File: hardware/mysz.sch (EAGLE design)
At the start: 30 parts, among them IC1 LM1117T(H)-3.3, IC2 LM1117T(H)-3.3, U1 NUCLEO-L053R8

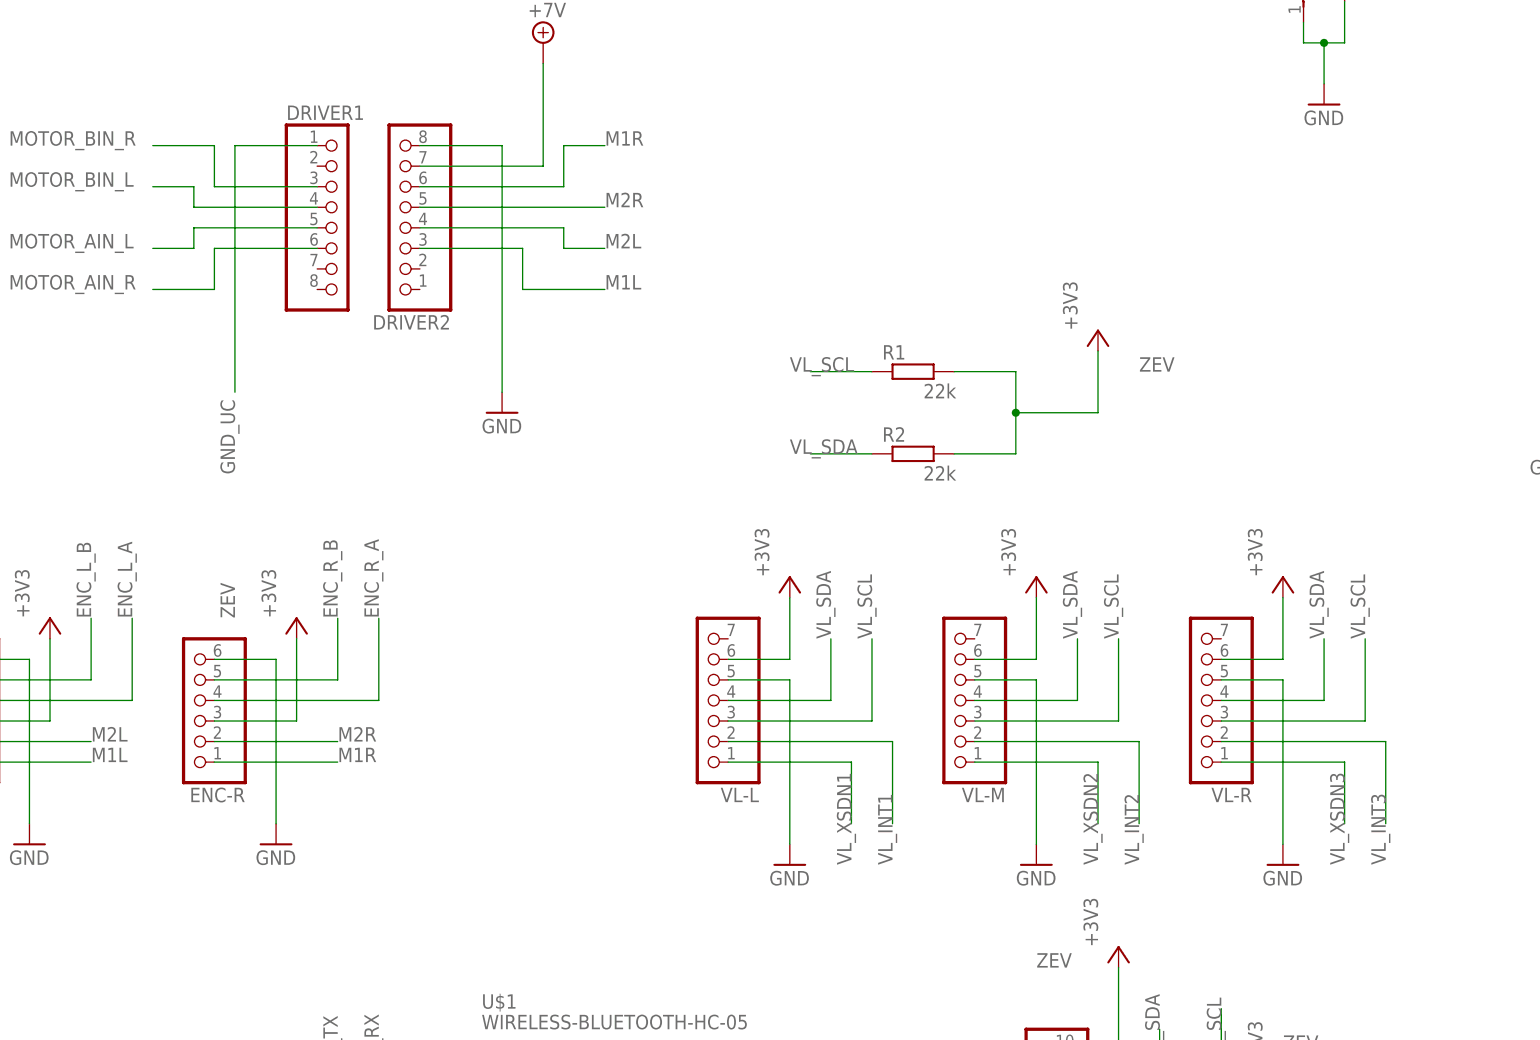
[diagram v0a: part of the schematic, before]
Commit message: Added missing links.sch
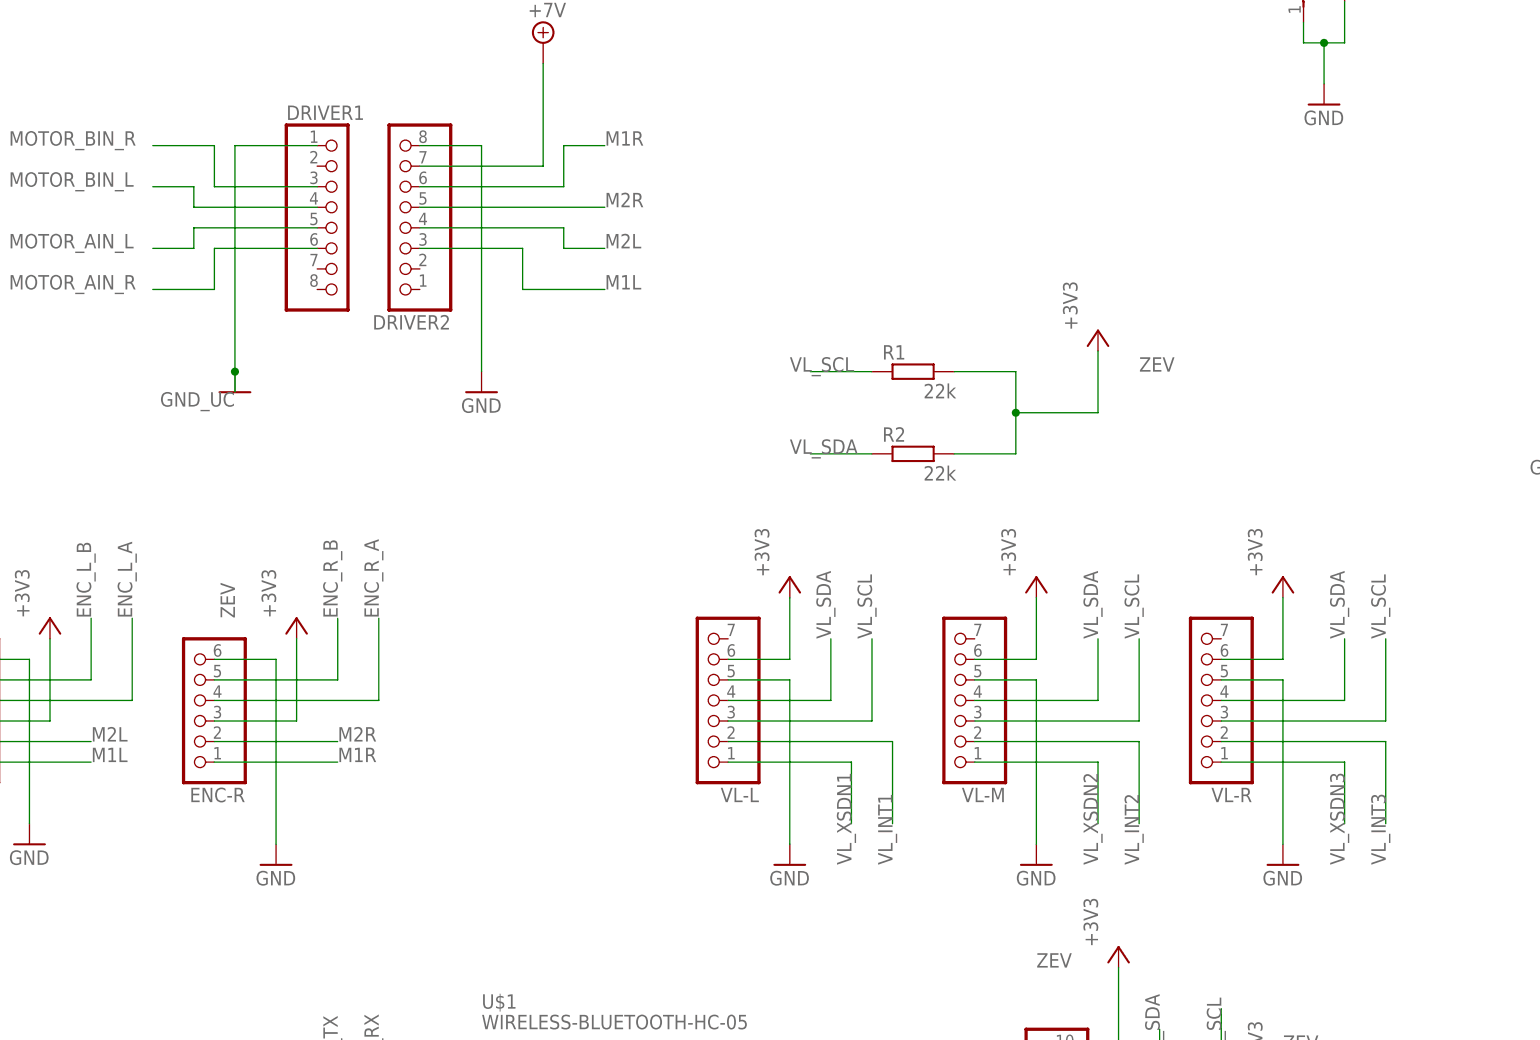
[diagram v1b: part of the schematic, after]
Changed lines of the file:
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@@
 <part name="+3V13" library="supply1" library_urn="urn:adsk.eagle:library:371" deviceset="+3V3" device=""/>
 <part name="C9" library="capacitor-wima" library_urn="urn:adsk.eagle:library:116" deviceset="C" device="2,5-3" package3d_urn="urn:adsk.eagle:package:5436/1" value="100nF"/>
+<part name="GND13" library="supply1" library_urn="urn:adsk.eagle:library:371" deviceset="GND" device=""/>
 </parts>
 <sheets>
@@
 <attribute name="VALUE" x="7.62" y="83.82" size="1.778" layer="96" rot="R90"/>
 </instance>
-<instance part="GND4" gate="1" x="7.62" y="55.88" smashed="yes">
-<attribute name="VALUE" x="5.08" y="53.34" size="1.778" layer="96"/>
+<instance part="GND4" gate="1" x="7.62" y="53.34" smashed="yes">
+<attribute name="VALUE" x="5.08" y="50.8" size="1.778" layer="96"/>
 </instance>
 <instance part="GND5" gate="1" x="71.12" y="53.34" smashed="yes">
@@
 <attribute name="VALUE" x="29.21" y="147.32" size="1.778" layer="96" rot="R180"/>
 </instance>
-<instance part="GND9" gate="1" x="35.56" y="109.22" smashed="yes">
-<attribute name="VALUE" x="33.02" y="106.68" size="1.778" layer="96"/>
+<instance part="GND9" gate="1" x="33.02" y="111.76" smashed="yes">
+<attribute name="VALUE" x="30.48" y="109.22" size="1.778" layer="96"/>
 </instance>
 <instance part="SUPPLY2" gate="G$1" x="40.64" y="154.94" smashed="yes">
@@
 <attribute name="VALUE" x="141.224" y="160.401" size="1.778" layer="96"/>
 </instance>
+<instance part="GND13" gate="1" x="2.54" y="111.76" smashed="yes"/>
 </instances>
 <busses>
@@
 <pinref part="ENC-R" gate="A" pin="6"/>
 <wire x1="0" y1="78.74" x2="7.62" y2="78.74" width="0.1524" layer="91"/>
-<wire x1="7.62" y1="78.74" x2="7.62" y2="58.42" width="0.1524" layer="91"/>
+<wire x1="7.62" y1="78.74" x2="7.62" y2="55.88" width="0.1524" layer="91"/>
 <pinref part="GND4" gate="1" pin="GND"/>
 </segment>
@@
 <segment>
 <pinref part="DRIVER2" gate="A" pin="8"/>
-<wire x1="25.4" y1="142.24" x2="35.56" y2="142.24" width="0.1524" layer="91"/>
-<wire x1="35.56" y1="142.24" x2="35.56" y2="111.76" width="0.1524" layer="91"/>
+<wire x1="25.4" y1="142.24" x2="33.02" y2="142.24" width="0.1524" layer="91"/>
+<wire x1="33.02" y1="142.24" x2="33.02" y2="114.3" width="0.1524" layer="91"/>
 <pinref part="GND9" gate="1" pin="GND"/>
 </segment>
@@
 <segment>
 <pinref part="VL-M" gate="A" pin="4"/>
-<wire x1="93.98" y1="73.66" x2="106.68" y2="73.66" width="0.1524" layer="91"/>
-<wire x1="106.68" y1="73.66" x2="106.68" y2="81.28" width="0.1524" layer="91"/>
-<label x="106.68" y="81.28" size="1.778" layer="95" rot="R90"/>
+<wire x1="93.98" y1="73.66" x2="109.22" y2="73.66" width="0.1524" layer="91"/>
+<wire x1="109.22" y1="73.66" x2="109.22" y2="81.28" width="0.1524" layer="91"/>
+<label x="109.22" y="81.28" size="1.778" layer="95" rot="R90"/>
 </segment>
 <segment>
 <pinref part="VL-R" gate="A" pin="4"/>
-<wire x1="124.46" y1="73.66" x2="137.16" y2="73.66" width="0.1524" layer="91"/>
-<wire x1="137.16" y1="73.66" x2="137.16" y2="81.28" width="0.1524" layer="91"/>
-<label x="137.16" y="81.28" size="1.778" layer="95" rot="R90"/>
+<wire x1="124.46" y1="73.66" x2="139.7" y2="73.66" width="0.1524" layer="91"/>
+<wire x1="139.7" y1="73.66" x2="139.7" y2="81.28" width="0.1524" layer="91"/>
+<label x="139.7" y="81.28" size="1.778" layer="95" rot="R90"/>
 </segment>
 <segment>
@@
 <segment>
 <pinref part="VL-M" gate="A" pin="3"/>
-<wire x1="93.98" y1="71.12" x2="111.76" y2="71.12" width="0.1524" layer="91"/>
-<wire x1="111.76" y1="71.12" x2="111.76" y2="81.28" width="0.1524" layer="91"/>
-<label x="111.76" y="81.28" size="1.778" layer="95" rot="R90"/>
+<wire x1="93.98" y1="71.12" x2="114.3" y2="71.12" width="0.1524" layer="91"/>
+<wire x1="114.3" y1="71.12" x2="114.3" y2="81.28" width="0.1524" layer="91"/>
+<label x="114.3" y="81.28" size="1.778" layer="95" rot="R90"/>
 </segment>
 <segment>
 <pinref part="VL-R" gate="A" pin="3"/>
-<wire x1="124.46" y1="71.12" x2="142.24" y2="71.12" width="0.1524" layer="91"/>
-<wire x1="142.24" y1="71.12" x2="142.24" y2="81.28" width="0.1524" layer="91"/>
-<label x="142.24" y="81.28" size="1.778" layer="95" rot="R90"/>
+<wire x1="124.46" y1="71.12" x2="144.78" y2="71.12" width="0.1524" layer="91"/>
+<wire x1="144.78" y1="71.12" x2="144.78" y2="81.28" width="0.1524" layer="91"/>
+<label x="144.78" y="81.28" size="1.778" layer="95" rot="R90"/>
 </segment>
 <segment>
@@
 <pinref part="DRIVER1" gate="A" pin="1"/>
 <wire x1="12.7" y1="142.24" x2="2.54" y2="142.24" width="0.1524" layer="91"/>
-<wire x1="2.54" y1="142.24" x2="2.54" y2="111.76" width="0.1524" layer="91"/>
-<label x="2.54" y="101.6" size="1.778" layer="95" rot="R90"/>
-</segment>
-<segment>
+<wire x1="2.54" y1="142.24" x2="2.54" y2="114.3" width="0.1524" layer="91"/>
+<label x="2.54" y="111.76" size="1.778" layer="95" rot="R180"/>
+<pinref part="GND13" gate="1" pin="GND"/>
+<wire x1="2.54" y1="114.3" x2="2.54" y2="111.76" width="0.1524" layer="91"/>
+<junction x="2.54" y="114.3"/>
+</segment>
+<segment>
